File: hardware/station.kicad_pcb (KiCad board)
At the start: 2 copper layers, 100 x 100.8 mm, 166 parts, among them J1 AudioJack3, J2 AudioJack3, J3 Conn_02x05_Odd_Even, J4 Conn_02x05_Odd_Even, Q1 NTMFS5C682NL, Q2 NTMFS5C682NL, Q3 FDV301N, Q4 FDV301N, Q5 DMP2120U, Q6 DMP2120U, Q7 NTMFS5C682NL, Q8 NTMFS5C682NL, U1 NCS213, U10 LM5109BSD, U11 STM32G431CBT6, U2 MAX44246, U3 LM5109BSD, U4 NCP700BSN30T1G, U5 MCP1501T-25E, U6 LM5164DDAR, U7 LM63615-Q1PWP, U8 NCS213, U9 MAX44246

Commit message: Some minor layout changes.
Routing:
- net (no net): track 25.5 -> 0.00 mm
- net Net-(C49-Pad1): track 0.00 -> 18.9 mm
- net /Microcontroller/CHB_LO: track 43.1 -> 50.6 mm
- net /Microcontroller/CHB_HI: track 44.2 -> 51.1 mm
- net /Microcontroller/CHB_TEMP: track 14.2 -> 10.9 mm
- net /Microcontroller/LCD_BL: track 36.2 -> 39.0 mm
- net /Microcontroller/CHB_VOL: track 28.8 -> 26.4 mm
- net +3V0: track 88.8 -> 91.1 mm
- net VREF: track 54.4 -> 56.4 mm
- net /Microcontroller/CHB_CUR: track 24.4 -> 22.5 mm
- net /Microcontroller/LCD_RS: track 38.4 -> 40.0 mm
- net /Microcontroller/LCD_SCL: track 45.4 -> 46.6 mm
- net Net-(C12-Pad1): vias 19 -> 29
- net GND: vias 25 -> 24
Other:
- rule via_min_size: 0.4 -> 0.3

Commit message: Layout almost complete. Just needs a tidy.
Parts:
- removed JP1, JP4: SolderJumper_2_Open, station:SolderJumper-2_6A
- removed the REF** at (98.2, 116.6)
- added F1: Fuse, station:Fuse_2410, F.Cu at (97.5, 86.5)
- added F2: Fuse, Fuse:Fuse_1206_3216Metric, F.Cu at (101.7, 88.4)
- added J5: Screw_Terminal_01x02, TerminalBlock:TerminalBlock_bornier-2_P5.08mm, B.Cu at (102.5, 91.4)
- added REF**: OSHW-Logo_5.7x6mm_SilkScreen, Symbol:OSHW-Logo_5.7x6mm_SilkScreen, F.Cu at (144.6, 90.0)
- added Ref**: Val**, station:IocesLogo, F.Cu at (146.5, 76.3)
- J4: value Conn_02x05_Odd_Even -> Conn_02x05_Counter_Clockwise; footprint Connector_PinHeader_2.54mm:PinHeader_2x05_P2.54mm_Vertical -> Connector:Tag-Connect_TC2050-IDC-NL_2x05_P1.27mm_Vertical
- moved Q5 113.7 mm to (145.6, 100.1)
- moved R35 113.6 mm to (145.6, 97.6)
- moved C36 113.6 mm to (148.5, 99.5)
- moved Q3 113.2 mm to (145.6, 95.1)
- moved R33 113.1 mm to (148.2, 95.7)
- moved R31 112.4 mm to (142.3, 96.0), turned to 0 degrees
- moved C28 96.7 mm to (54.9, 94.5), turned to 180 degrees
- moved U5 93.6 mm to (55.4, 99.2), turned to 270 degrees
- moved R27 93.6 mm to (55.7, 96.5)
- moved C23 91.3 mm to (55.6, 102.2), turned to 180 degrees
- moved Q4 84.9 mm to (96.0, 103.8), turned to 90 degrees
- moved R32 82.3 mm to (94.5, 106.3), turned to 0 degrees
- moved R34 82.0 mm to (97.5, 106.3), turned to 0 degrees
- moved C37 81.2 mm to (98.9, 103.2)
- moved R36 80.0 mm to (101.8, 106.3)
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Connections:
- C12 pad 1: Net-(C12-Pad1) -> +V_PWR
- C13 pad 1: Net-(C12-Pad1) -> +V_PWR
- C14 pad 1: Net-(C12-Pad1) -> +V_PWR
- C15 pad 1: Net-(C12-Pad1) -> +V_PWR
- C18 pad 1: Net-(C12-Pad1) -> +V_PWR
- C49 pad 1: Net-(C49-Pad1) -> +V_PWR
- C50 pad 1: Net-(C49-Pad1) -> +V_PWR
- C51 pad 1: Net-(C49-Pad1) -> +V_PWR
- C52 pad 1: Net-(C49-Pad1) -> +V_PWR
- C55 pad 1: Net-(C49-Pad1) -> +V_PWR
- J4 pad 9: GND -> /Microcontroller/~TRST
- Q1 pad 5: Net-(C12-Pad1) -> +V_PWR
- Q7 pad 5: Net-(C49-Pad1) -> +V_PWR
- R31 pad 1: /Power/EN_12V -> /Microcontroller/EN_12V
- R32 pad 1: /Power/EN_3V3 -> /Microcontroller/EN_3V3
- U11 pad 10: /Microcontroller/CHA_TEMP -> /Microcontroller/CHB_TEMP
- U11 pad 11: /Microcontroller/CHB_VOL -> /Microcontroller/CHA_VOL
- U11 pad 12: /Microcontroller/CHB_CUR -> /Microcontroller/CHA_CUR
- U11 pad 13: /Microcontroller/CHB_TEMP -> /Microcontroller/CHA_TEMP
- U11 pad 41: /Microcontroller/TRST -> /Microcontroller/~TRST
- U11 pad 5: Net-(U11-Pad5) -> /Microcontroller/EN_12V
- U11 pad 6: Net-(U11-Pad6) -> /Microcontroller/EN_3V3
- U11 pad 8: /Microcontroller/CHA_VOL -> /Microcontroller/CHB_VOL
- U11 pad 9: /Microcontroller/CHA_CUR -> /Microcontroller/CHB_CUR
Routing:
- net VREF: track 56.4 -> 243.9 mm, vias 6 -> 8
- net +3V0: track 91.1 -> 276.6 mm, vias 4 -> 6
- net /Microcontroller/CHB_VOL: track 26.4 -> 156.7 mm, vias 1 -> 2
- net /Microcontroller/CHB_TEMP: track 10.9 -> 140.3 mm, vias 1 -> 2
- net /Microcontroller/CHB_CUR: track 22.5 -> 151.0 mm, vias 1 -> 2
- net +12V: track 15.2 -> 127.5 mm, vias 0 -> 7
- net +3V3_STBY: track 56.0 -> 153.9 mm, vias 3 -> 6
- net /Microcontroller/EN_12V: track 0.00 -> 94.2 mm, vias 0 -> 6
- net /Microcontroller/BAT_VOL: track 3.54 -> 75.5 mm, vias 0 -> 2
- net /Microcontroller/CHA_HI: track 7.00 -> 62.4 mm
- net /Microcontroller/CHA_TEMP: track 10.9 -> 66.2 mm, vias 1 -> 2
- net /Microcontroller/CHA_CUR: track 22.5 -> 76.6 mm, vias 1 -> 2
- net /Microcontroller/CHA_VOL: track 26.4 -> 79.8 mm, vias 1 -> 2
- net /Microcontroller/CHA_LO: track 6.16 -> 58.7 mm
- net +3V3: track 20.5 -> 71.5 mm, vias 1 -> 4
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- added copper zone on B.Cu, net +V_PWR
- added copper zone on F.Cu, net +V_PWR
- added copper zone on B.Cu, net /Channel A/RET
- added copper zone on B.Cu, net /Channel B/RET
- removed copper zone on B.Cu, net Net-(C12-Pad1)
- removed copper zone on F.Cu, net Net-(C12-Pad1)
- removed copper zone on B.Cu, net Net-(C49-Pad1)
- removed copper zone on F.Cu, net Net-(C49-Pad1)
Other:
- board size 100 x 100.8 mm -> 100 x 60 mm
- net class Default: trace_width 0.25 -> 0.2; via_dia 0.8 -> 0.6; via_drill 0.4 -> 0.3
- net class HV added: clearance 0.6, trace_width 0.2, via_dia 0.6, via_drill 0.3
- board text added: "Flux v1.0.0"

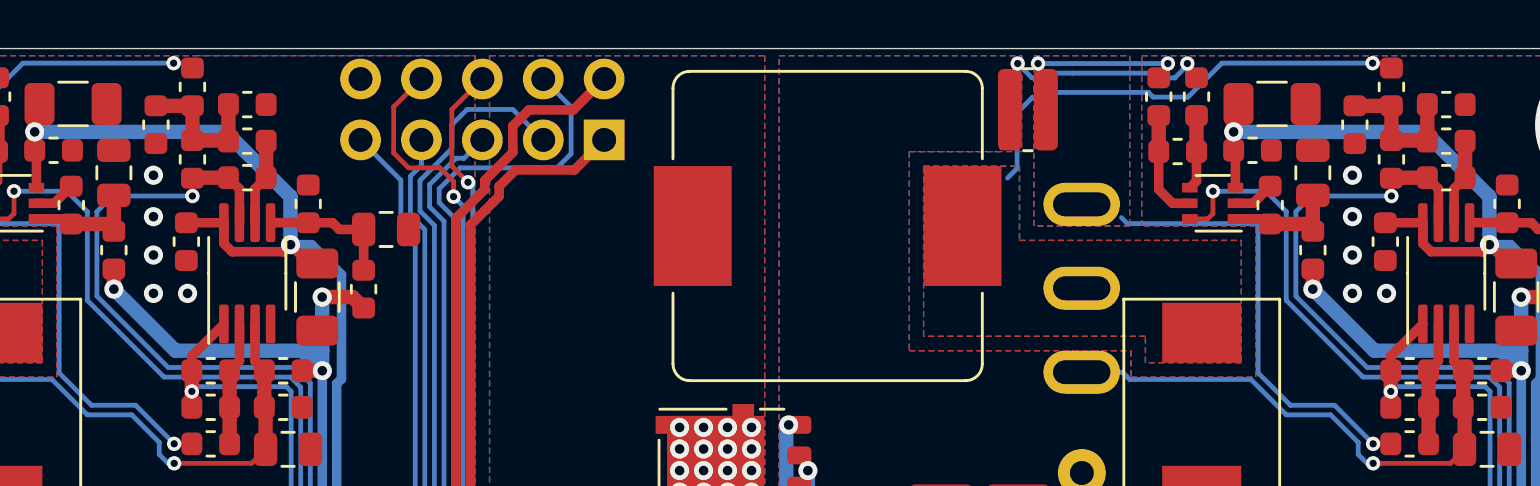
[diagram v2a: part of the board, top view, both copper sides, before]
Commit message: Remove some vias to prep for plugin stitching.
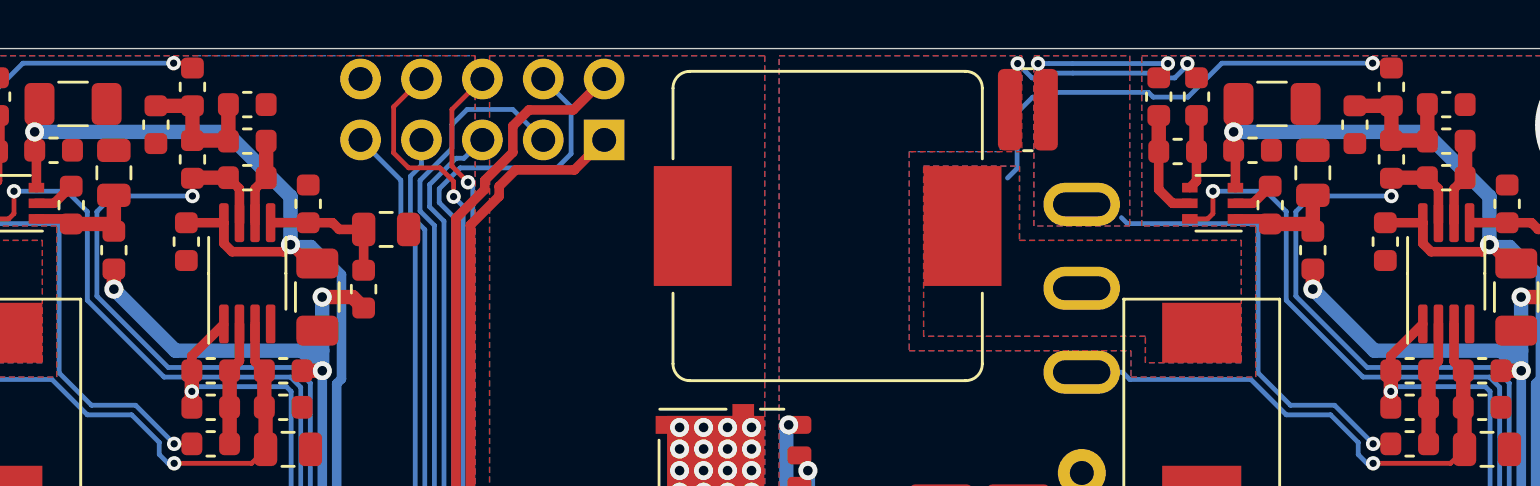
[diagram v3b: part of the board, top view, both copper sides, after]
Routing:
- net GND: vias 22 -> 12

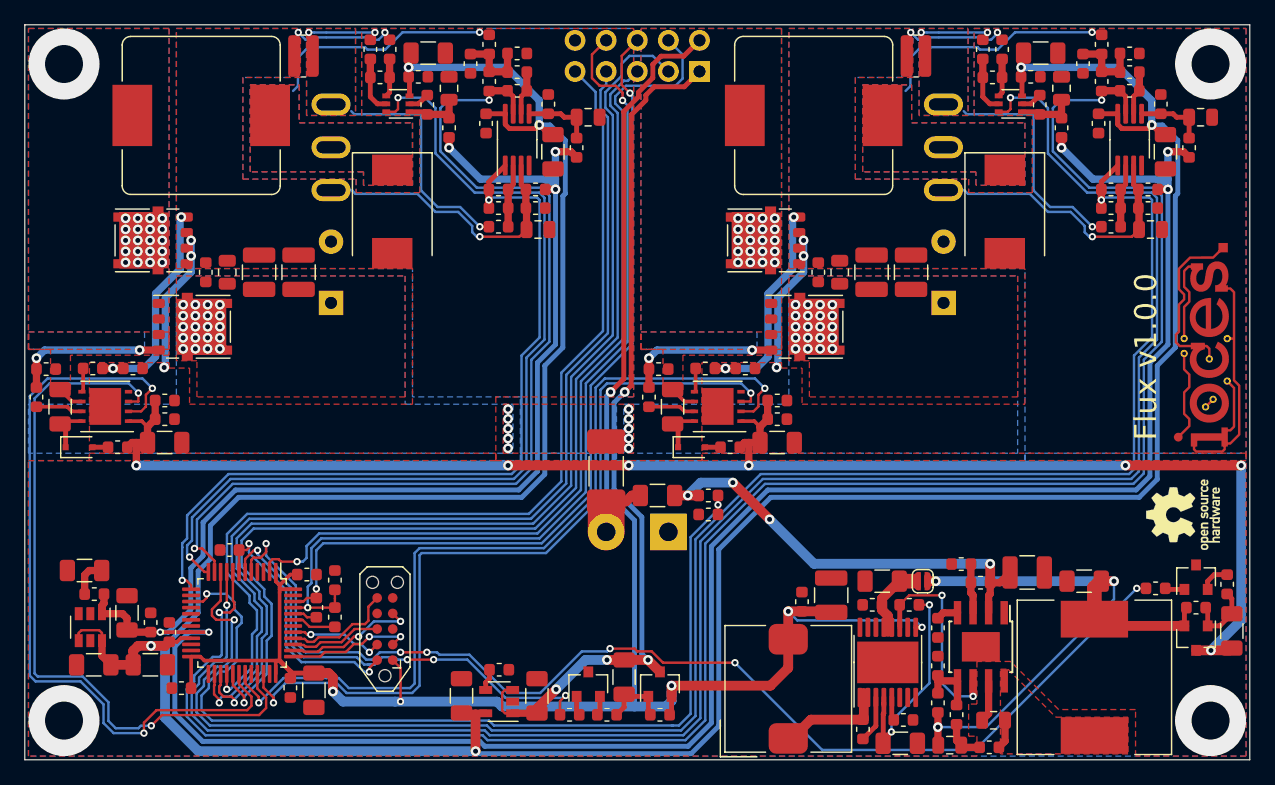
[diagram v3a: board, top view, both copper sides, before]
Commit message: Add stitching vias
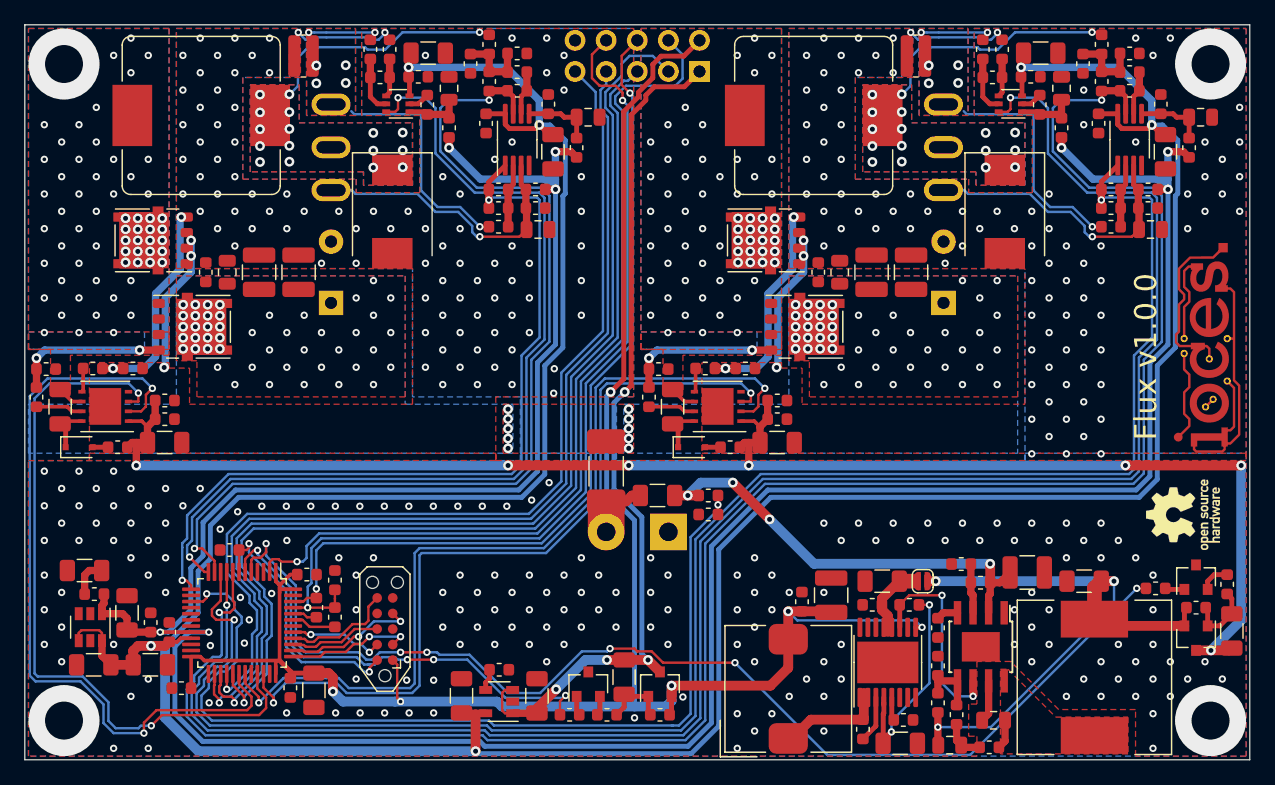
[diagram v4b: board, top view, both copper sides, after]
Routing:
- net Net-(C9-Pad1): vias 20 -> 60
- net Net-(C46-Pad1): vias 20 -> 63
- net GND: vias 12 -> 364
- net /Channel B/RET: vias 2 -> 6
- net /Channel B/HEAT: vias 1 -> 17
- net /Channel A/RET: vias 2 -> 6
- net /Channel A/HEAT: vias 1 -> 17
- net +V_PWR: vias 50 -> 102
- net (no net): vias 0 -> 1
